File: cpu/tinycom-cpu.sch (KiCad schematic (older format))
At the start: 10 parts, among them P1 CONN_02X08, P2 CONN_02X08, U1 OLIMEX_IC_A13, U2 H5TQ2G83BFR/FBGA82, Y1 Crystal

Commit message: router power
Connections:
- net SDC0_CLK: now also P1.7 (P7); no longer P1.5 (P5)
- net SDC0_CMD: now also P1.5 (P5); no longer P1.7 (P7)
- net SDC0_D0: now also P1.9 (P9); no longer P1.3 (P3)
- net SDC0_D1: now also P1.11 (P11); no longer P1.1 (P1)
- net SDC0_D2: now also P1.1 (P1); no longer P1.11 (P11)
- net SDC0_D3: now also P1.3 (P3); no longer P1.9 (P9)
- net UART1_RX: now also P1.13 (P13); no longer P1.15 (P15)
- net UART1_TX: now also P1.15 (P15); no longer P1.13 (P13)
- net at C2.1, U1.91 (X24MOUT): now also Y1.1; no longer Y1.2
- net at C1.1, U1.92 (X24MIN): now also Y1.2; no longer Y1.1
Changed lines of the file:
@@
 UDM0
 Text GLabel 7350 5400 0    60   Input ~ 0
+SDC0_D2
+Text GLabel 7350 5500 0    60   Input ~ 0
+SDC0_D3
+Text GLabel 7350 5600 0    60   Input ~ 0
+SDC0_CMD
+Text GLabel 7350 5700 0    60   Input ~ 0
+SDC0_CLK
+Text GLabel 7350 5800 0    60   Input ~ 0
+SDC0_D0
+Text GLabel 7350 5900 0    60   Input ~ 0
 SDC0_D1
-Text GLabel 7350 5500 0    60   Input ~ 0
-SDC0_D0
-Text GLabel 7350 5600 0    60   Input ~ 0
-SDC0_CLK
-Text GLabel 7350 5700 0    60   Input ~ 0
-SDC0_CMD
-Text GLabel 7350 5800 0    60   Input ~ 0
-SDC0_D3
-Text GLabel 7350 5900 0    60   Input ~ 0
-SDC0_D2
 Text GLabel 7850 5400 2    60   Input ~ 0
 UDM0
@@
 CSI_D7
 Text GLabel 7350 6000 0    60   Input ~ 0
+UART1_RX
+Text GLabel 7350 6100 0    60   Input ~ 0
 UART1_TX
-Text GLabel 7350 6100 0    60   Input ~ 0
-UART1_RX
 Text GLabel 9400 6100 2    60   Input ~ 0
 GND
@@
 F 3 "" H 1250 2000 60  0000 C CNN
 	1    1250 2000
-	0    1    1    0
+	0    -1   -1   0
 $EndComp
 $Comp
@@
 	1500 1900 1500 1850
 Wire Wire Line
-	1500 1850 900  1850
-Wire Wire Line
 	1650 2100 1450 2100
 Wire Wire Line
-	1450 2100 1450 2150
-Wire Wire Line
-	1450 2150 900  2150
+	1450 2150 1450 2100
 Connection ~ 1250 1850
 Connection ~ 1250 2150
@@
 Wire Wire Line
 	6400 4200 6400 4250
+Wire Wire Line
+	1500 1850 900  1850
+Wire Wire Line
+	900  2150 1450 2150
 $EndSCHEMATC

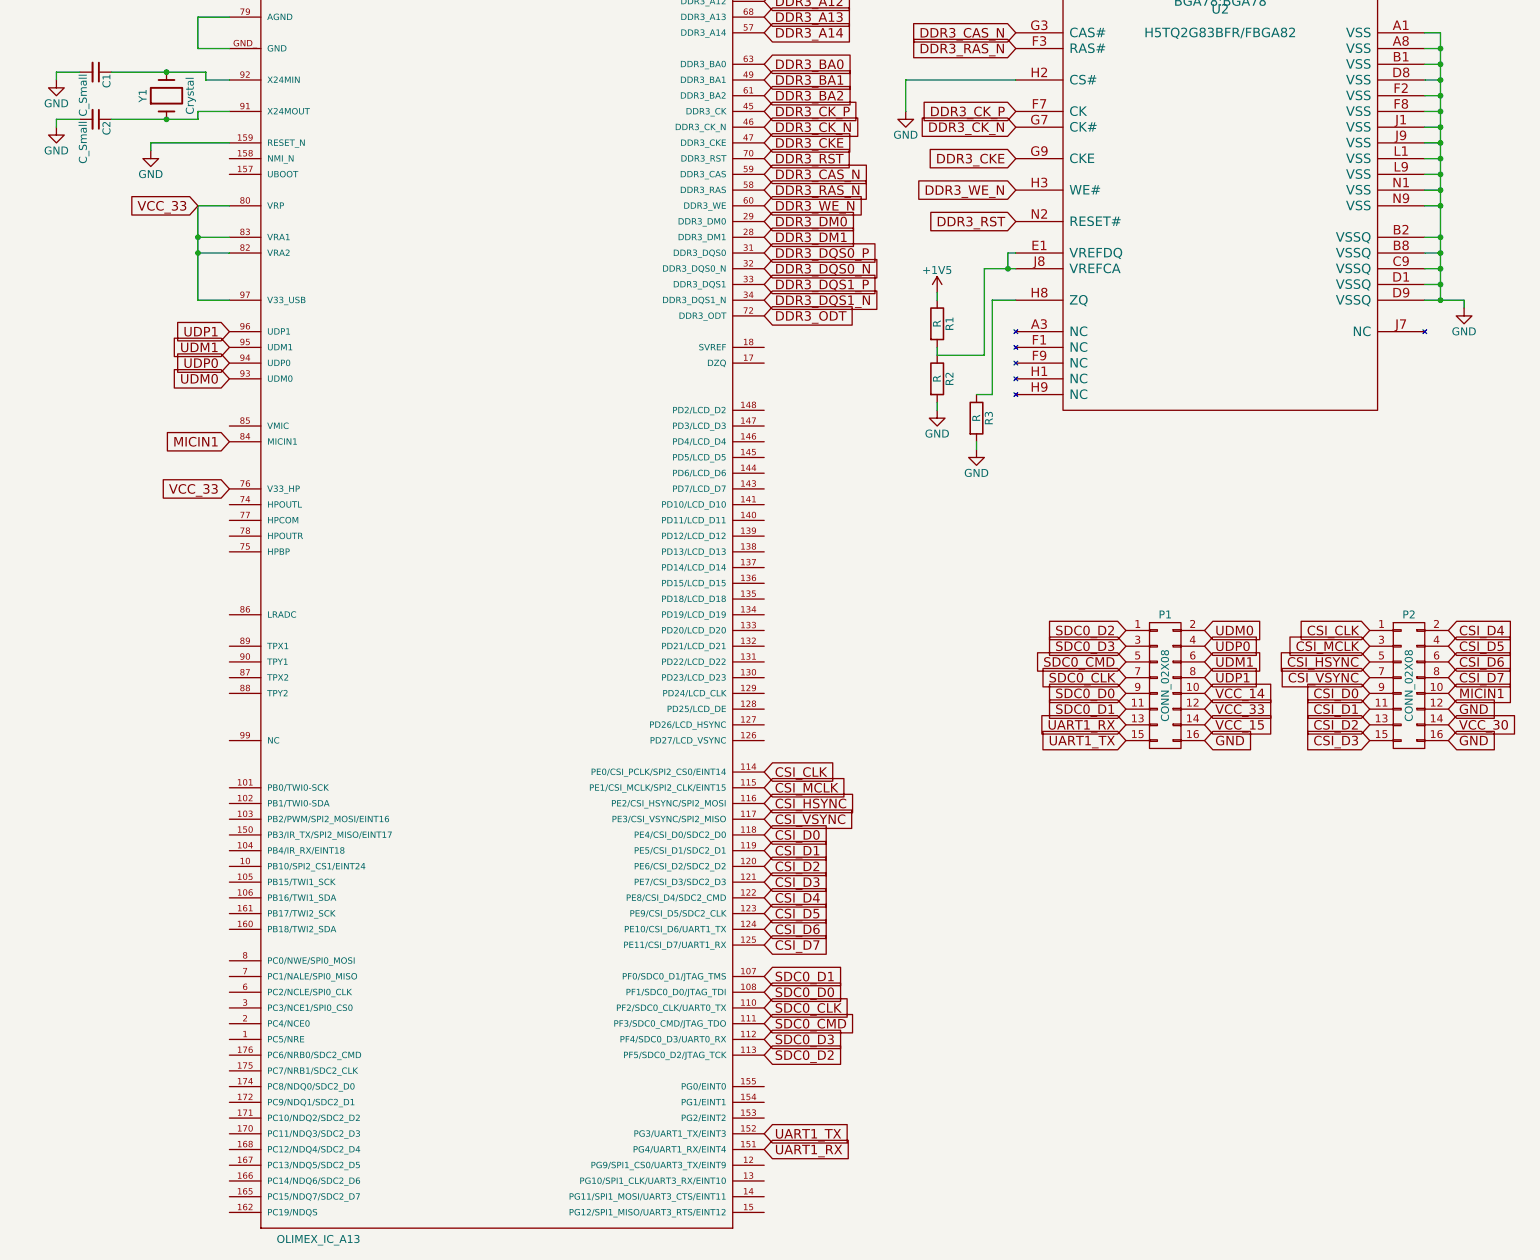
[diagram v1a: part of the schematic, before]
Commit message: add missing routes in ddr
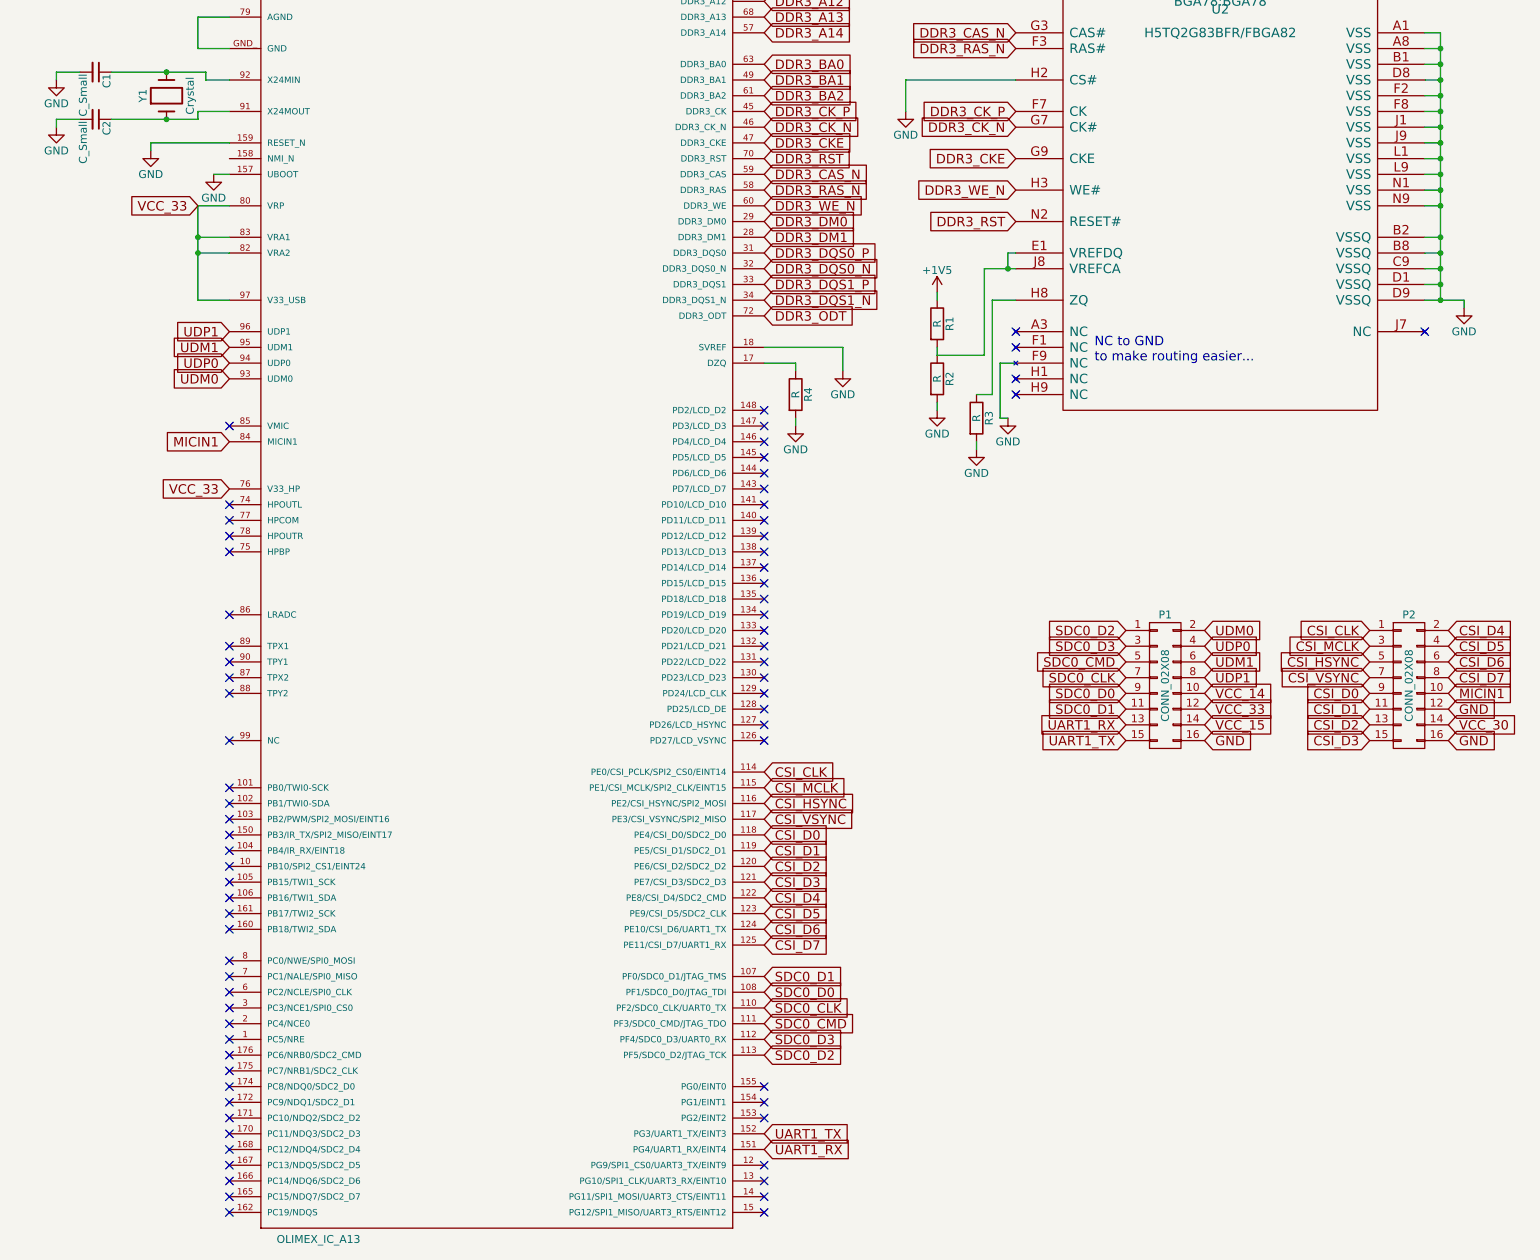
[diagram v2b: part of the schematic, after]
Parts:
- added R4: R, Resistors_SMD:R_0603, symbol R
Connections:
- net GND: now also U1.157 (UBOOT), U1.18 (SVREF), U2.F9 (NC), R4.2
- net at U1.17 (DZQ): now also R4.1
- no-connect marks 0 -> 72
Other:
- note added: "NC to GND\nto make routing easier..."
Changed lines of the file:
@@
 	1650 2100 1450 2100
 Wire Wire Line
-	1450 2150 1450 2100
+	1450 2100 1450 2150
 Connection ~ 1250 1850
 Connection ~ 1250 2150
@@
 	1500 1850 900  1850
 Wire Wire Line
-	900  2150 1450 2150
+	1450 2150 900  2150
+NoConn ~ 6650 3500
+NoConn ~ 6650 3600
+NoConn ~ 6650 3800
+NoConn ~ 6650 3900
+NoConn ~ 9250 3500
+$Comp
+L GND #PWR012
+U 1 1 56261679
+P 6600 4050
+F 0 "#PWR012" H 6600 3800 50  0001 C CNN
+F 1 "GND" H 6600 3900 50  0000 C CNN
+F 2 "" H 6600 4050 60  0000 C CNN
+F 3 "" H 6600 4050 60  0000 C CNN
+	1    6600 4050
+	1    0    0    -1
+$EndComp
+Wire Wire Line
+	6650 3700 6550 3700
+Wire Wire Line
+	6550 3700 6550 4050
+Wire Wire Line
+	6550 4050 6600 4050
+Text Notes 7150 3700 0    60   ~ 0
+NC to GND\nto make routing easier...
+NoConn ~ 5050 4000
+NoConn ~ 5050 4100
+NoConn ~ 5050 4200
+NoConn ~ 5050 4300
+NoConn ~ 5050 4400
+NoConn ~ 5050 4500
+NoConn ~ 5050 4600
+NoConn ~ 5050 4700
+NoConn ~ 5050 4800
+NoConn ~ 5050 4900
+NoConn ~ 5050 5000
+NoConn ~ 5050 5100
+NoConn ~ 5050 5200
+NoConn ~ 5050 5300
+NoConn ~ 5050 5400
+NoConn ~ 5050 5500
+NoConn ~ 5050 5600
+NoConn ~ 5050 5700
+NoConn ~ 5050 5800
+NoConn ~ 5050 5900
+NoConn ~ 5050 6000
+NoConn ~ 5050 6100
+NoConn ~ 5050 8300
+NoConn ~ 5050 8400
+NoConn ~ 5050 8500
+NoConn ~ 5050 8800
+NoConn ~ 5050 8900
+NoConn ~ 5050 9000
+NoConn ~ 5050 9100
+NoConn ~ 1650 7500
+NoConn ~ 1650 7600
+NoConn ~ 1650 7700
+NoConn ~ 1650 7800
+NoConn ~ 1650 7900
+NoConn ~ 1650 8000
+NoConn ~ 1650 8100
+NoConn ~ 1650 8200
+NoConn ~ 1650 8300
+NoConn ~ 1650 8400
+NoConn ~ 1650 8500
+NoConn ~ 1650 8600
+NoConn ~ 1650 8700
+NoConn ~ 1650 8800
+NoConn ~ 1650 8900
+NoConn ~ 1650 9000
+NoConn ~ 1650 9100
+NoConn ~ 1650 6400
+NoConn ~ 1650 6500
+NoConn ~ 1650 6600
+NoConn ~ 1650 6700
+NoConn ~ 1650 6800
+NoConn ~ 1650 6900
+NoConn ~ 1650 7000
+NoConn ~ 1650 7100
+NoConn ~ 1650 7200
+NoConn ~ 1650 7300
+NoConn ~ 1650 6100
+NoConn ~ 1650 5500
+NoConn ~ 1650 5600
+NoConn ~ 1650 5700
+NoConn ~ 1650 5800
+NoConn ~ 1650 5300
+NoConn ~ 1650 4900
+NoConn ~ 1650 4800
+NoConn ~ 1650 4700
+NoConn ~ 1650 4600
+NoConn ~ 1650 4100
+$Comp
+L GND #PWR013
+U 1 1 56262629
+P 1550 2500
+F 0 "#PWR013" H 1550 2250 50  0001 C CNN
+F 1 "GND" H 1550 2350 50  0000 C CNN
+F 2 "" H 1550 2500 60  0000 C CNN
+F 3 "" H 1550 2500 60  0000 C CNN
+	1    1550 2500
+	1    0    0    -1
+$EndComp
+Wire Wire Line
+	1650 2500 1550 2500
+$Comp
+L GND #PWR014
+U 1 1 56262930
+P 5550 3750
+F 0 "#PWR014" H 5550 3500 50  0001 C CNN
+F 1 "GND" H 5550 3600 50  0000 C CNN
+F 2 "" H 5550 3750 60  0000 C CNN
+F 3 "" H 5550 3750 60  0000 C CNN
+	1    5550 3750
+	1    0    0    -1
+$EndComp
+Wire Wire Line
+	5050 3600 5550 3600
+$Comp
+L R R4
+U 1 1 56262A08
+P 5250 3900
+F 0 "R4" V 5330 3900 50  0000 C CNN
+F 1 "R" V 5250 3900 50  0000 C CNN
+F 2 "Resistors_SMD:R_0603" V 5180 3900 30  0001 C CNN
+F 3 "" H 5250 3900 30  0000 C CNN
+	1    5250 3900
+	1    0    0    -1
+$EndComp
+Wire Wire Line
+	5050 3700 5250 3700
+Wire Wire Line
+	5250 3700 5250 3750
+Wire Wire Line
+	5550 3600 5550 3750
+$Comp
+L GND #PWR015
+U 1 1 56262D84
+P 5250 4100
+F 0 "#PWR015" H 5250 3850 50  0001 C CNN
+F 1 "GND" H 5250 3950 50  0000 C CNN
+F 2 "" H 5250 4100 60  0000 C CNN
+F 3 "" H 5250 4100 60  0000 C CNN
+	1    5250 4100
+	1    0    0    -1
+$EndComp
+Wire Wire Line
+	5250 4050 5250 4100
 $EndSCHEMATC

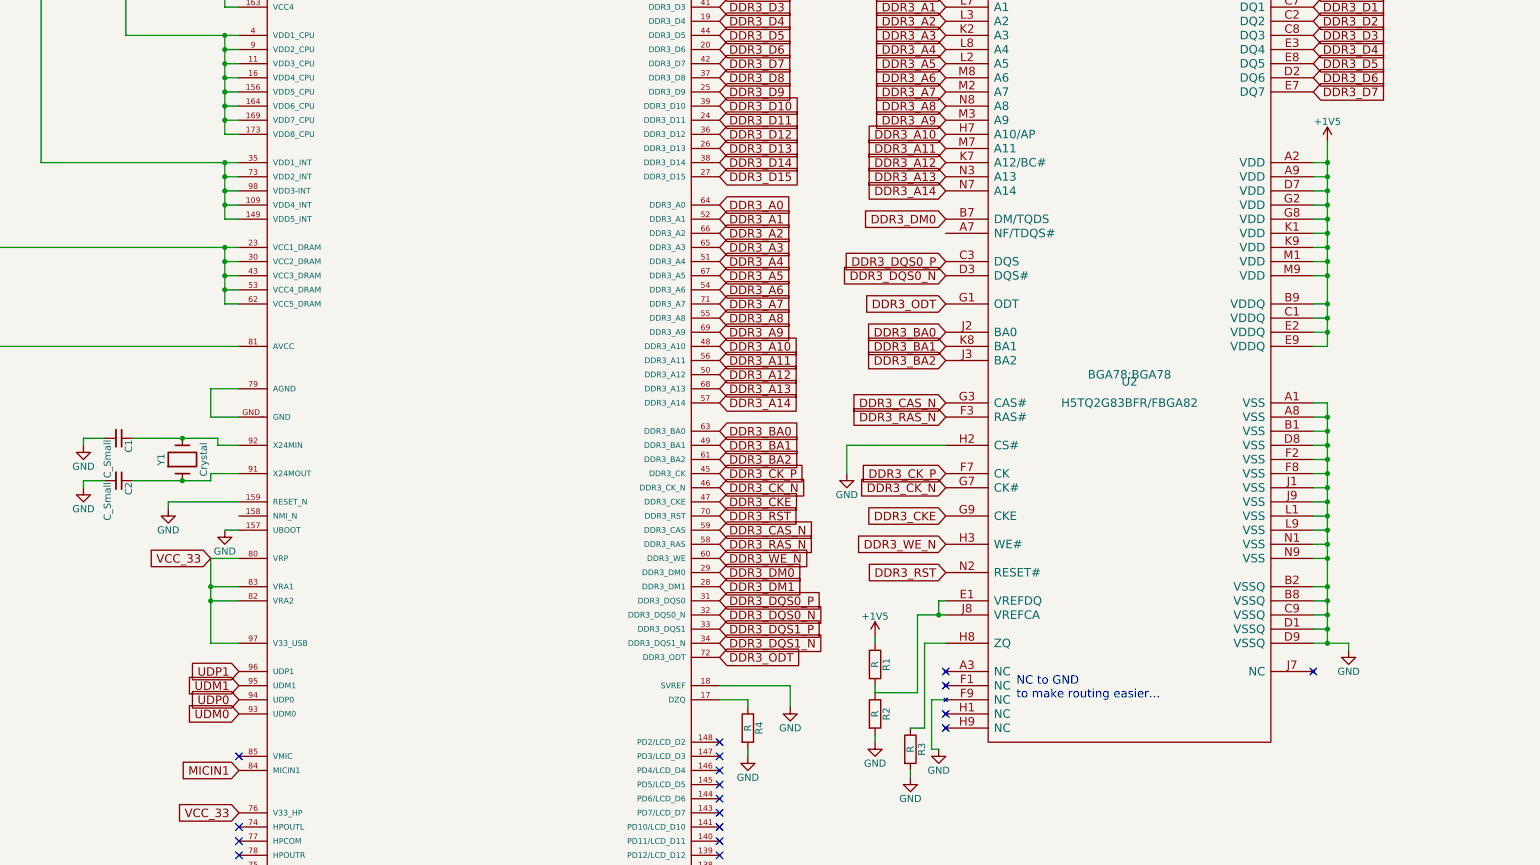
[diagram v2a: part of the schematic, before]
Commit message: add some capacitors
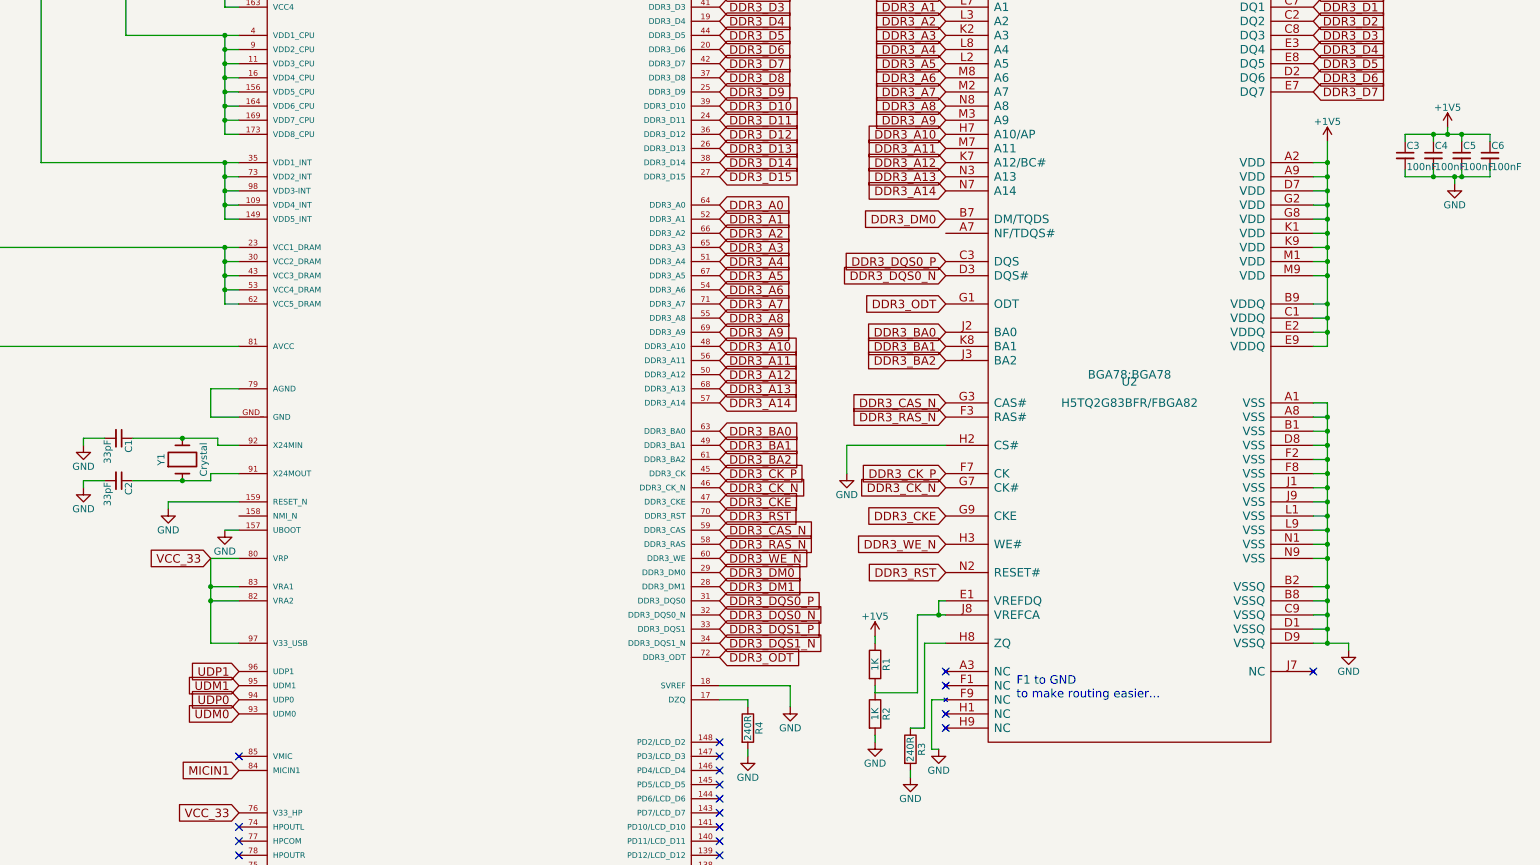
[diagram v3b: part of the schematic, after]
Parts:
- added C3, C4, C5, C6: 100nF, Capacitors_SMD:C_0603, symbol C_Small
- C1, C2: value C_Small -> 33pF
- R1, R2: value R -> 1K
- R3, R4: value R -> 240R
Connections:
- net +1V5: now also C3.1, C4.1, C5.1, C6.1
- net GND: now also C3.2, C4.2, C5.2, C6.2
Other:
- note added: "F1 to GND\nto make routing easier..."
- note removed: "NC to GND\nto make routing easier..."
